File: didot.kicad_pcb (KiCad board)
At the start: 2 copper layers, 151.1 x 116.8 mm, 69 parts, among them J1 JST_BATTERY, U1 nice!nano

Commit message: Add footprints / pretty library
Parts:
- removed G***: LOGO, Didot:DidotMark_Right

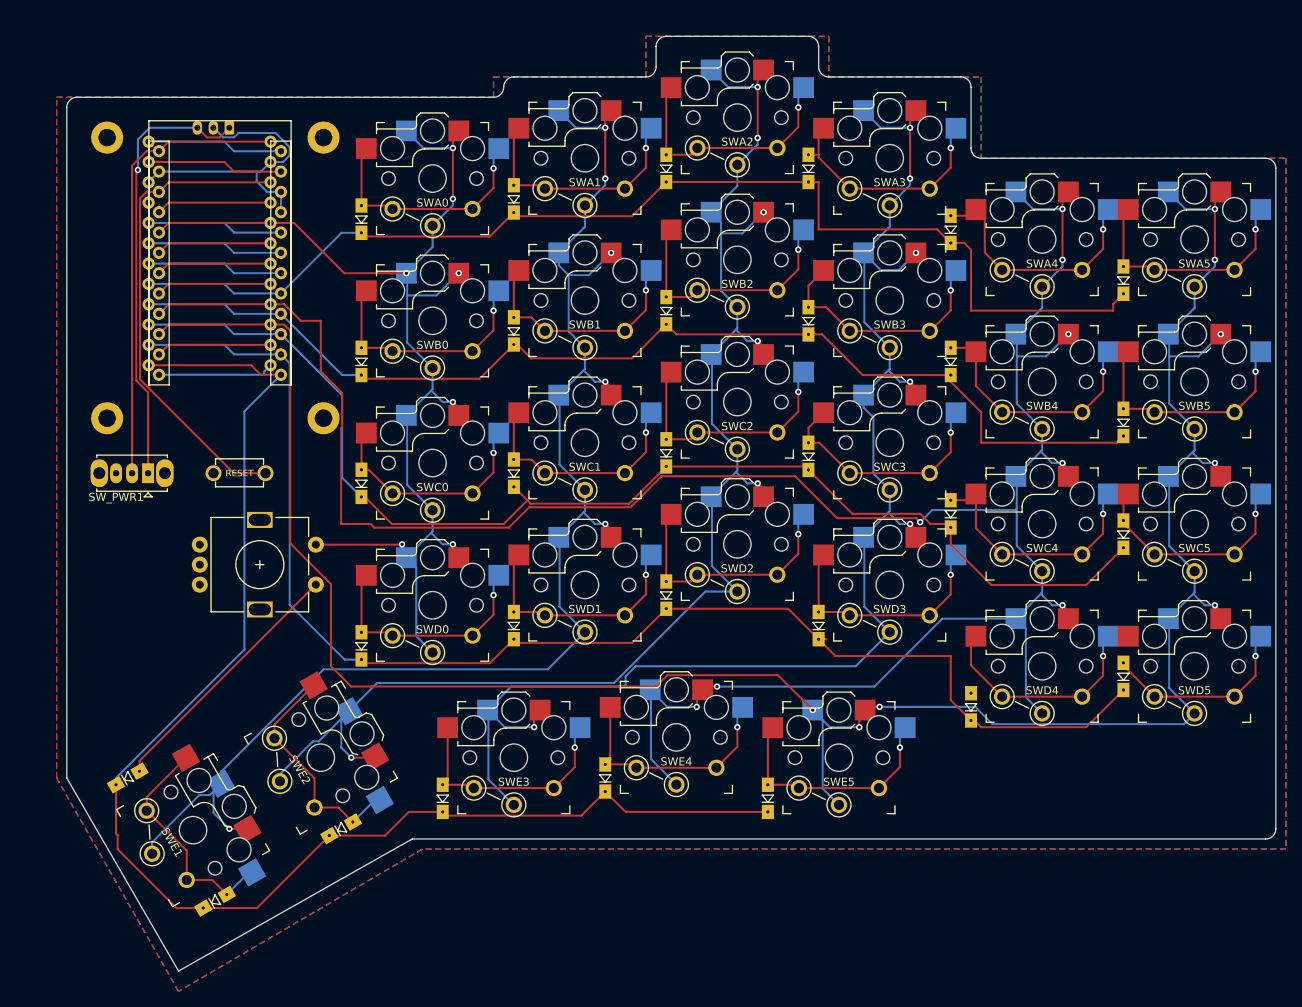
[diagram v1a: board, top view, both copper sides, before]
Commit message: enlarge board outline
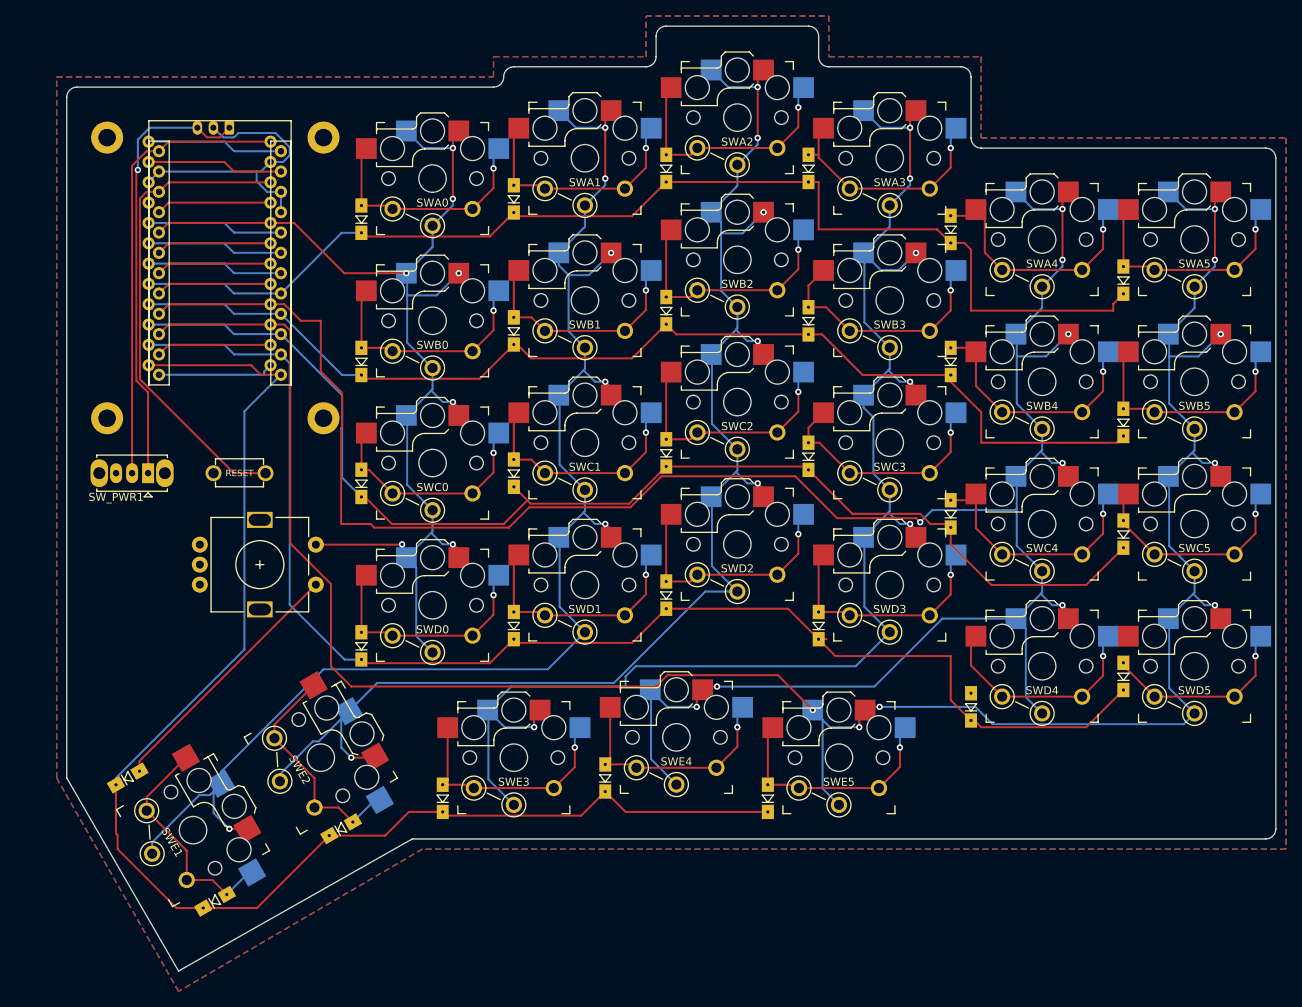
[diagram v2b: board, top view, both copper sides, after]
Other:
- board size 151.1 x 116.8 mm -> 151.1 x 118.1 mm

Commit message: Finish rewiring of keys
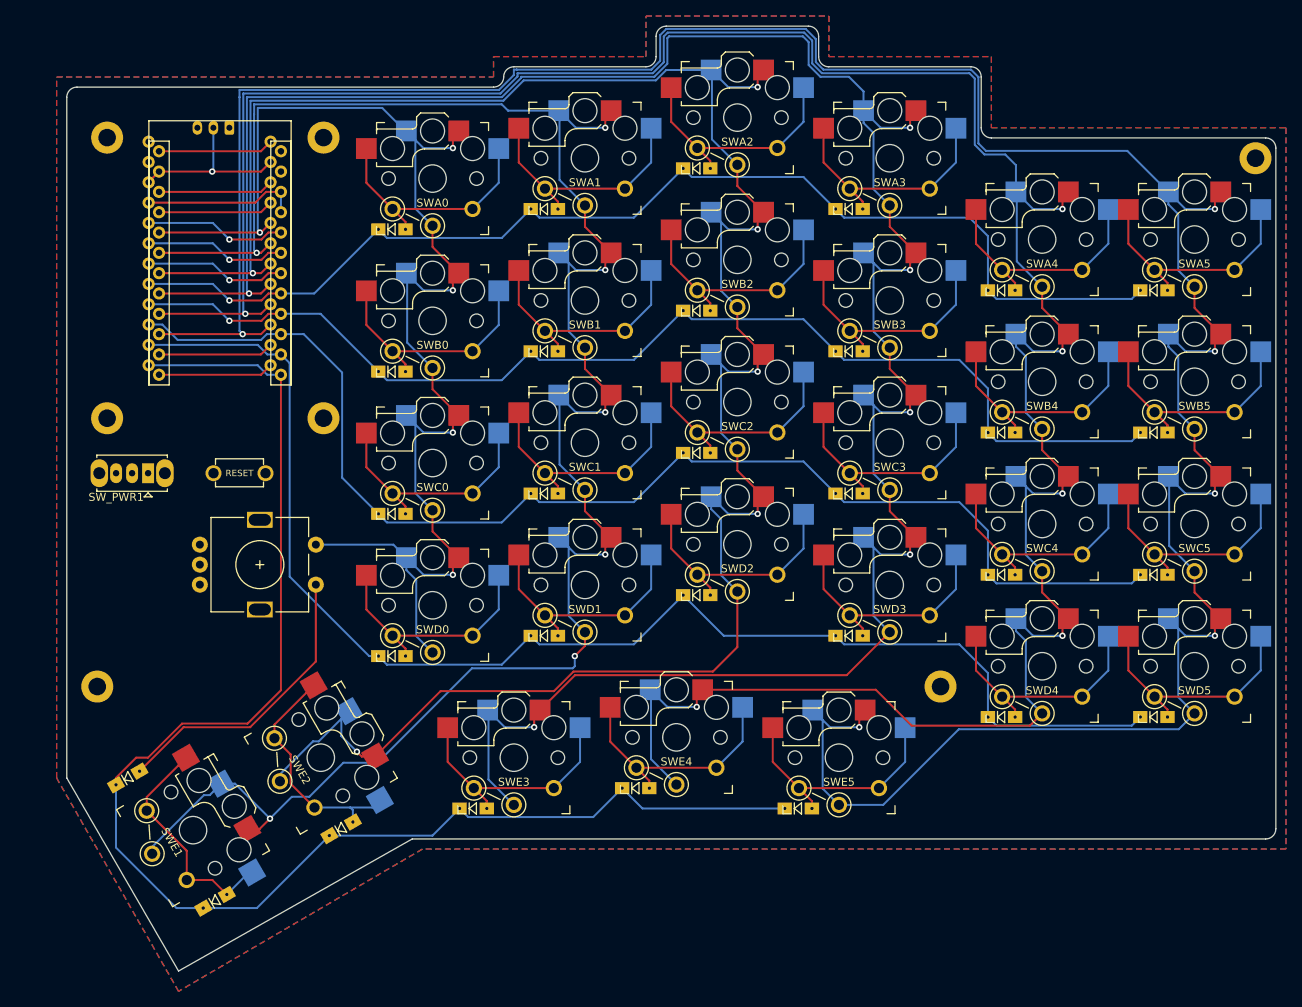
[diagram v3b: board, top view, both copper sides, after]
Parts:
- added TH1: HOLE, Didot:M2_HOLE_PCB, F.Cu at (66.0, 102.9)
- added TH1: HOLE, Didot:M2_HOLE_PCB, F.Cu at (210.8, 36.8)
- added TH1: HOLE, Didot:M2_HOLE_PCB, F.Cu at (171.4, 102.9)
- moved DB4 10.9 mm to (179.1, 71.1), turned to 0 degrees
- moved DA4 9.92 mm to (179.1, 53.3), turned to 0 degrees
- moved DC4 9.92 mm to (179.1, 88.9), turned to 0 degrees
- moved DA3 7.18 mm to (160.0, 43.2), turned to 0 degrees
- moved DC3 6.89 mm to (160.0, 78.7), turned to 0 degrees
- moved DB3 6.35 mm to (160.0, 61.0), turned to 0 degrees
- moved DC5 6.35 mm to (198.1, 88.9), turned to 0 degrees
- moved DD5 6.35 mm to (198.1, 106.7), turned to 0 degrees
- moved DC0 5.39 mm to (102.9, 81.3), turned to 0 degrees
- moved DB1 4.58 mm to (121.9, 61.0), turned to 0 degrees
- moved DC1 4.58 mm to (121.9, 78.7), turned to 0 degrees
- moved DB5 4.02 mm to (198.1, 71.1), turned to 0 degrees
- moved DD4 4.02 mm to (179.1, 106.7), turned to 0 degrees
- moved DA1 4.02 mm to (121.9, 43.2), turned to 0 degrees
- moved DA5 4.02 mm to (198.1, 53.3), turned to 0 degrees
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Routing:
- net col3: track 193.0 -> 309.6 mm
- net col2: track 191.9 -> 286.0 mm
- net col5: track 294.3 -> 364.7 mm, vias 8 -> 6
- net col1: track 192.9 -> 259.0 mm, vias 6 -> 7
- net Net-(J1-Pad1): track 55.5 -> 0.00 mm, vias 1 -> 0
- net RESET: track 60.3 -> 14.4 mm
- net VCC: track 57.0 -> 14.4 mm
- net col4: track 307.4 -> 340.0 mm, vias 8 -> 6
- net col0: track 148.3 -> 173.1 mm, vias 7 -> 5
- net Net-(U1-Pad2): track 17.0 -> 0.00 mm
- net Net-(U1-Pad1): track 17.0 -> 0.00 mm
- net rowE: track 176.8 -> 185.6 mm
- net Net-(DD5-Pad2): track 24.7 -> 31.0 mm, vias 1 -> 0
- net Net-(DE0-Pad2): track 32.4 -> 37.3 mm
- net rowC: track 153.5 -> 157.4 mm
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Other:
- outline, holes or cut-outs redrawn

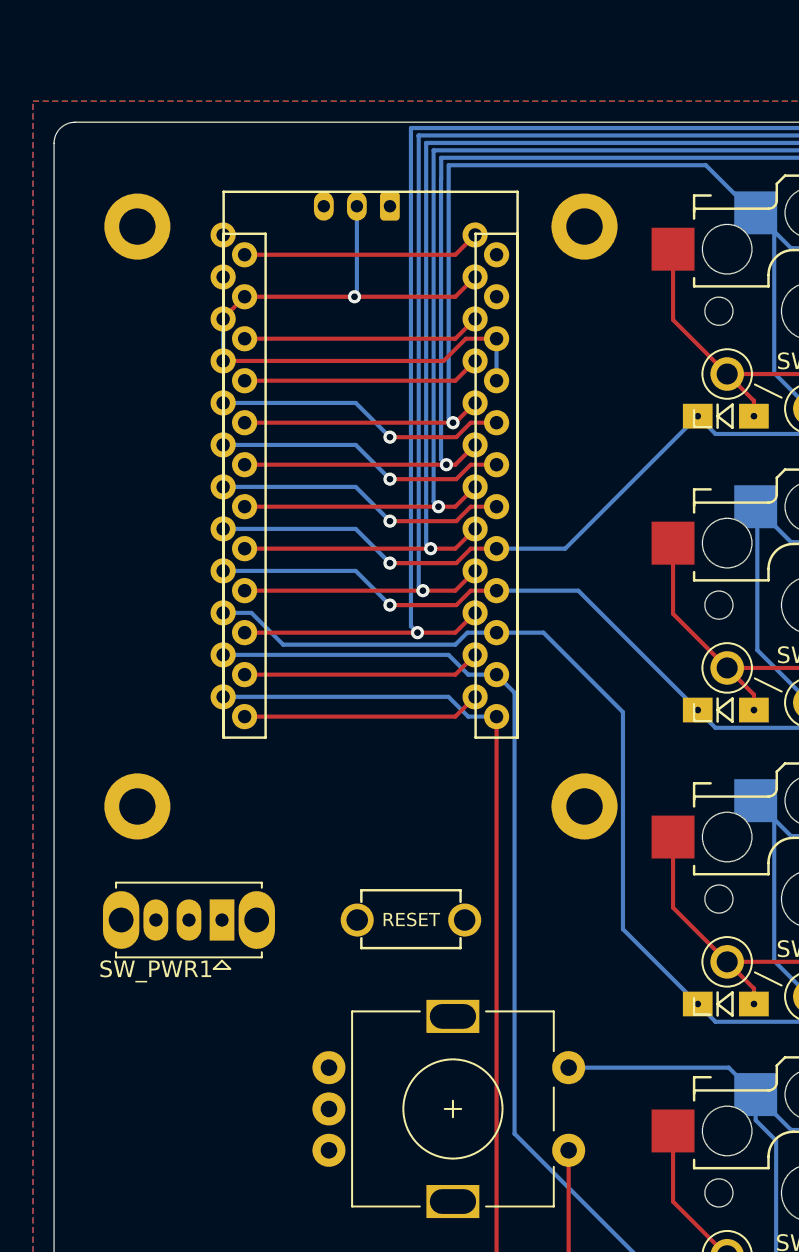
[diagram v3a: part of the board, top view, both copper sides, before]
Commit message: Use waveshare display footprint
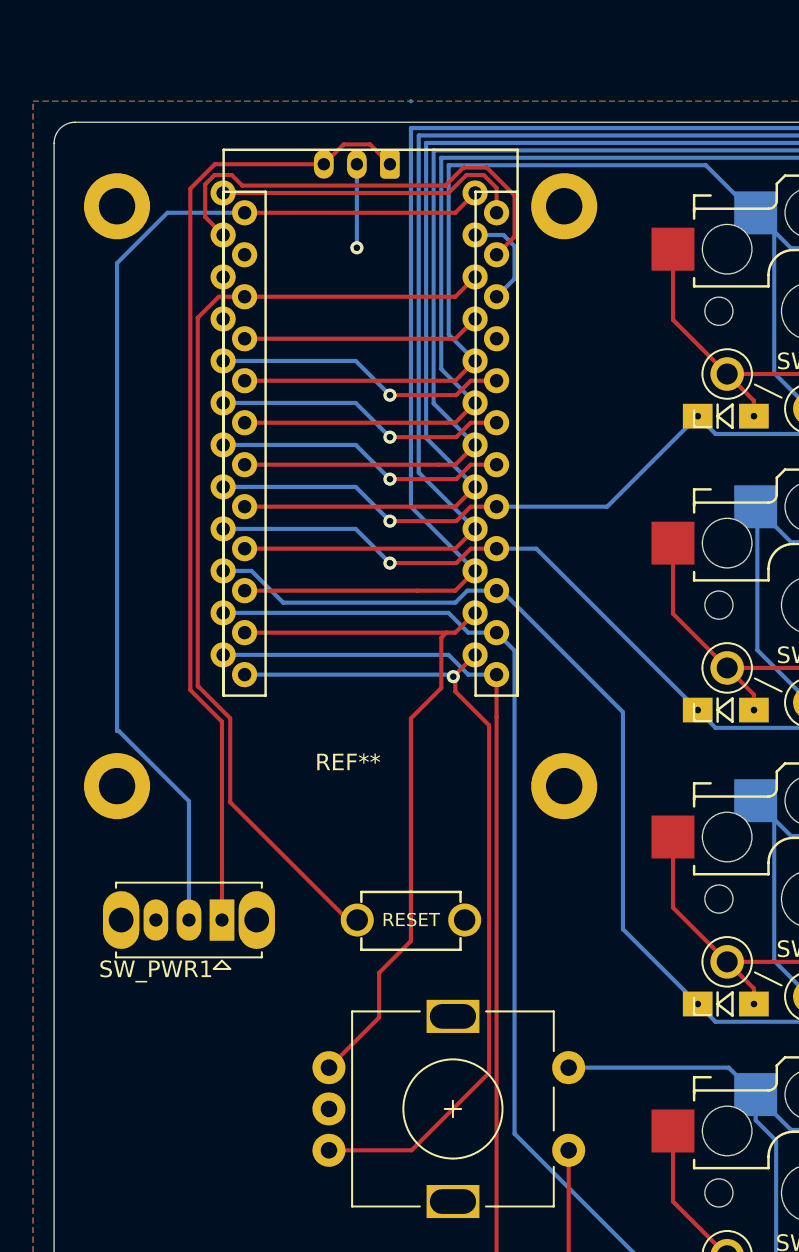
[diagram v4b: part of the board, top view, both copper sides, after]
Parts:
- removed the TH1 at (67.3, 34.2)
- removed TH2, TH3, TH4: HOLE, Didot:M2_HOLE_PCB
- added REF**: Waveshare_Sharp_LCD, Didot:Waveshare_Sharp_LCD, F.Cu at (66.0, 33.0)
- moved J1 2.54 mm to (82.5, 30.5)
- moved U1 2.54 mm to (81.3, 47.0)
- turned SW_RESET1 to 180 degrees
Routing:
- net Net-(J1-Pad1): track 0.00 -> 58.7 mm
- net VCC: track 14.4 -> 65.0 mm
- net RESET: track 14.4 -> 58.6 mm
- net ENCB: track 14.4 -> 50.9 mm, vias 0 -> 1
- net GND: track 44.0 -> 13.8 mm
- net ENCA: track 14.4 -> 43.9 mm
- net Net-(U1-Pad2): track 0.00 -> 27.9 mm
- net Net-(U1-Pad1): track 0.00 -> 18.8 mm
- net col0: track 173.1 -> 170.0 mm, vias 5 -> 4
- net col1: track 259.0 -> 255.9 mm, vias 7 -> 6
- net col2: track 286.0 -> 283.2 mm, vias 6 -> 5
- net col3: track 309.6 -> 307.0 mm, vias 6 -> 5
- net rowE: track 185.6 -> 188.2 mm
- net rowD: track 171.1 -> 173.6 mm
- net col4: track 340.0 -> 337.6 mm, vias 6 -> 5
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
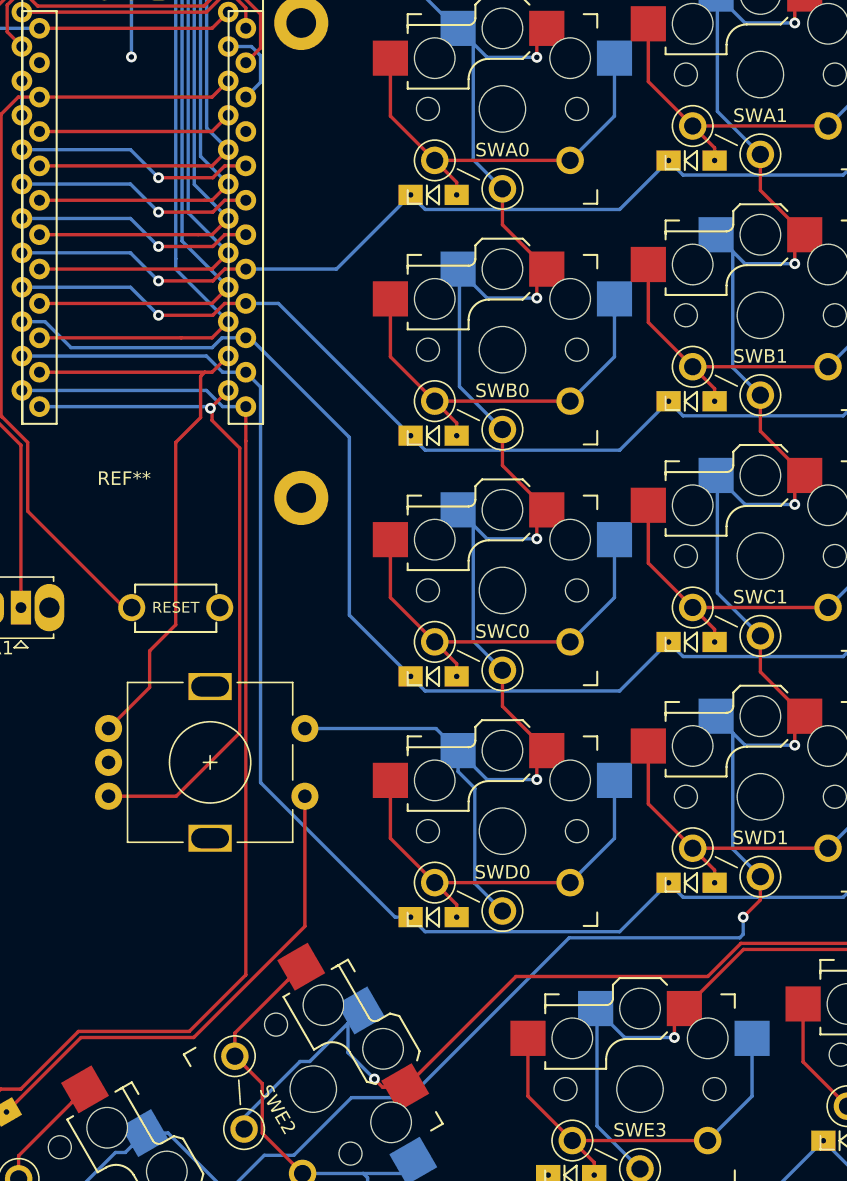
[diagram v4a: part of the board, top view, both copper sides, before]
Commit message: Clean up routing, add JST pin markings
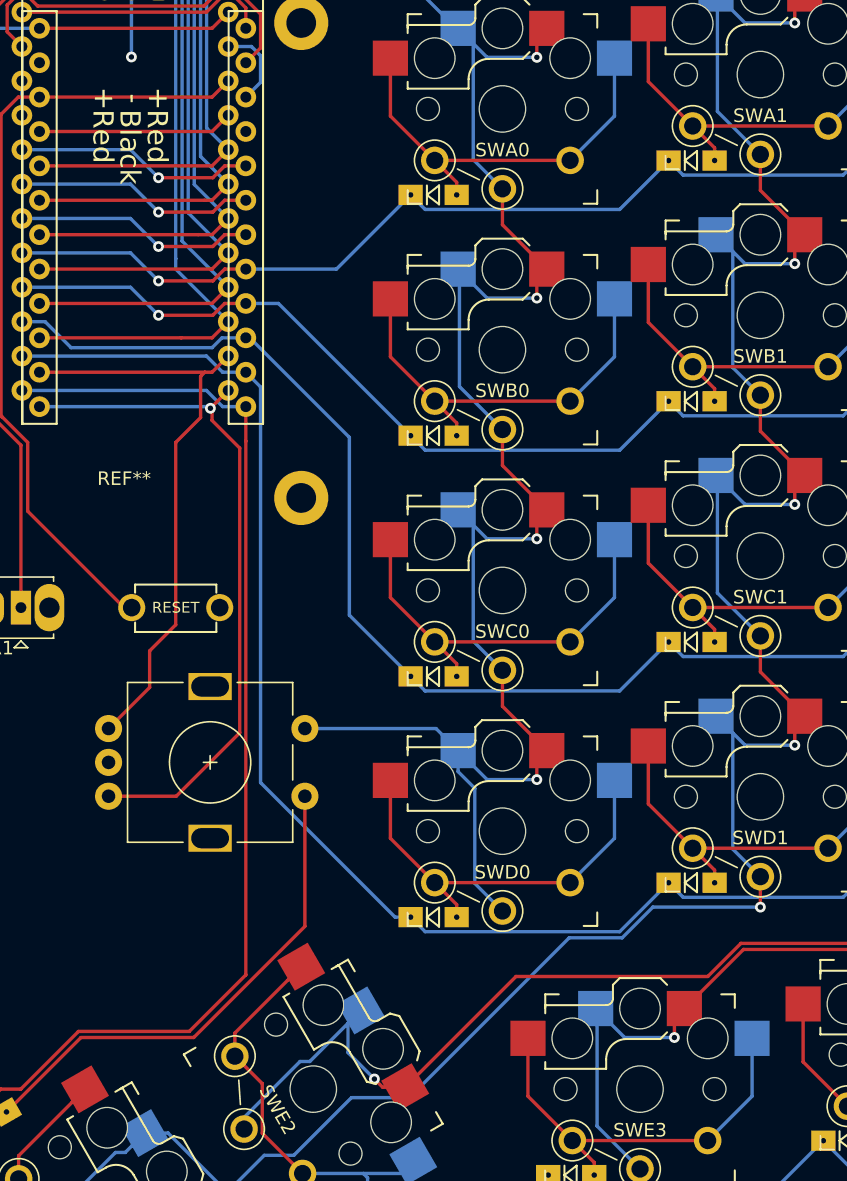
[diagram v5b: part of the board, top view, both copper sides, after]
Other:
- board text added: "+"
- board text added: "-"
- board text added: "Black"
- board text added: "Red"
